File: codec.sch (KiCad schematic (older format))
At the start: 15 parts, among them U4 TLV320AIC3101

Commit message: Use a better codec
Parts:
- removed TP1: MIC1LP/LINE1LP, symbol Connector:TestPoint_Probe
- removed TP2: HPLCOM, symbol Connector:TestPoint_Probe
- removed TP3: HPLOUT, symbol Connector:TestPoint_Probe
- removed TP4: LEFT_LOM, symbol Connector:TestPoint_Probe
- removed TP5: LEFT_LOP, symbol Connector:TestPoint_Probe
- removed U4: TLV320AIC3101, Package_DFN_QFN:QFN-32-1EP_5x5mm_P0.5mm_EP3.65x3.65mm, symbol Audio:TLV320AIC3101
- added C13: 0.1u, symbol Device:C
- added C14: 1u, symbol Device:C
- added C15: 10u, symbol Device:C
- added U2: WM8731SEDS, Package_SO:SSOP-28_5.3x10.2mm_P0.65mm, symbol Audio:WM8731SEDS
- C10, C12: value 1u -> 10u
- C11: value 0.1u -> 10u
- C6: value 1u -> 0.1u
- C8: value 10u -> 1u
- C9: value 0.1u -> 1u
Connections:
- net labels added: ADC, AVDD, DAC, DBVDD, DCVDD, HPVDD, SCLK, SDIN, ~CSB
- net labels removed: 1.8V, DIN, DOUT, SCL, SDA, ~RESET
- no-connect marks 10 -> 9

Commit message: Various fixes
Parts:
- added R18: 10k, symbol Device:R
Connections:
- net 3.3V: now also R18.2; no longer U2.21 (MODE)
- new net: R18.1, U2.21 (MODE)
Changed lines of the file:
@@
 Wire Wire Line
 	5250 3950 5400 3950
-Text GLabel 5250 4250 0    50   Input ~ 0
-3.3V
-Wire Wire Line
-	5250 4250 5400 4250
+Text GLabel 4400 4250 0    50   Input ~ 0
+3.3V
 Text GLabel 1950 2650 0    50   Input ~ 0
 3.3V
@@
 Wire Wire Line
 	6300 3050 6300 3150
+$Comp
+L Device:R R18
+U 1 1 6039A986
+P 4650 4250
+F 0 "R18" V 4443 4250 50  0000 C CNN
+F 1 "10k" V 4534 4250 50  0000 C CNN
+F 2 "" V 4580 4250 50  0001 C CNN
+F 3 "~" H 4650 4250 50  0001 C CNN
+	1    4650 4250
+	0    1    1    0
+$EndComp
+Wire Wire Line
+	4500 4250 4400 4250
+Wire Wire Line
+	4800 4250 5400 4250
 $EndSCHEMATC

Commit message: Add debug interface
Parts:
- renumbered C13 to C21, C4 to C22, C5 to C23, C6 to C24, C14 to C25, C7 to C26, C8 to C27, C9 to C28, C15 to C29, C10 to C30, C11 to C31, C12 to C32, R18 to R19, U2 to U4
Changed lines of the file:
@@
 $EndDescr
 $Comp
-L Audio:WM8731SEDS U2
+L Audio:WM8731SEDS U4
 U 1 1 6005E3AC
 P 6100 4050
-F 0 "U2" H 5250 5100 50  0000 C CNN
+F 0 "U4" H 5250 5100 50  0000 C CNN
 F 1 "WM8731SEDS" H 5450 5000 50  0000 C CNN
 F 2 "Package_SO:SSOP-28_5.3x10.2mm_P0.65mm" H 6100 2750 50  0001 C CNN
@@
 $EndComp
 $Comp
-L power:GND #PWR07
+L power:GND #PWR035
 U 1 1 60067126
 P 5900 5050
-F 0 "#PWR07" H 5900 4800 50  0001 C CNN
+F 0 "#PWR035" H 5900 4800 50  0001 C CNN
 F 1 "GND" H 5905 4877 50  0000 C CNN
 F 2 "" H 5900 5050 50  0001 C CNN
@@
 Connection ~ 6200 5000
 $Comp
-L Device:C C13
+L Device:C C21
 U 1 1 600750C8
 P 2100 2900
-F 0 "C13" H 2215 2946 50  0000 L CNN
+F 0 "C21" H 2215 2946 50  0000 L CNN
 F 1 "0.1u" H 2215 2855 50  0000 L CNN
 F 2 "" H 2138 2750 50  0001 C CNN
@@
 $EndComp
 $Comp
-L Device:C C14
+L Device:C C25
 U 1 1 600750CE
 P 2550 2900
-F 0 "C14" H 2665 2946 50  0000 L CNN
+F 0 "C25" H 2665 2946 50  0000 L CNN
 F 1 "1u" H 2665 2855 50  0000 L CNN
 F 2 "" H 2588 2750 50  0001 C CNN
@@
 	2100 2650 2550 2650
 $Comp
-L Device:C C15
+L Device:C C29
 U 1 1 600750DE
 P 3000 2900
-F 0 "C15" H 3115 2946 50  0000 L CNN
+F 0 "C29" H 3115 2946 50  0000 L CNN
 F 1 "10u" H 3115 2855 50  0000 L CNN
 F 2 "" H 3038 2750 50  0001 C CNN
@@
 Connection ~ 2100 2650
 $Comp
-L power:GND #PWR08
+L power:GND #PWR031
 U 1 1 600DD992
 P 2550 3200
-F 0 "#PWR08" H 2550 2950 50  0001 C CNN
+F 0 "#PWR031" H 2550 2950 50  0001 C CNN
 F 1 "GND" H 2555 3027 50  0000 C CNN
 F 2 "" H 2550 3200 50  0001 C CNN
@@
 	5900 3050 5900 3150
 $Comp
-L Device:C C4
+L Device:C C22
 U 1 1 600E70B7
 P 2100 3800
-F 0 "C4" H 2215 3846 50  0000 L CNN
+F 0 "C22" H 2215 3846 50  0000 L CNN
 F 1 "0.1u" H 2215 3755 50  0000 L CNN
 F 2 "" H 2138 3650 50  0001 C CNN
@@
 $EndComp
 $Comp
-L Device:C C7
+L Device:C C26
 U 1 1 600E70BD
 P 2550 3800
-F 0 "C7" H 2665 3846 50  0000 L CNN
+F 0 "C26" H 2665 3846 50  0000 L CNN
 F 1 "1u" H 2665 3755 50  0000 L CNN
 F 2 "" H 2588 3650 50  0001 C CNN
@@
 	2100 3550 2550 3550
 $Comp
-L Device:C C10
+L Device:C C30
 U 1 1 600E70C9
 P 3000 3800
-F 0 "C10" H 3115 3846 50  0000 L CNN
+F 0 "C30" H 3115 3846 50  0000 L CNN
 F 1 "10u" H 3115 3755 50  0000 L CNN
 F 2 "" H 3038 3650 50  0001 C CNN
@@
 Connection ~ 2100 3550
 $Comp
-L power:GND #PWR09
+L power:GND #PWR032
 U 1 1 600E70D8
 P 2550 4100
-F 0 "#PWR09" H 2550 3850 50  0001 C CNN
+F 0 "#PWR032" H 2550 3850 50  0001 C CNN
 F 1 "GND" H 2555 3927 50  0000 C CNN
 F 2 "" H 2550 4100 50  0001 C CNN
@@
 Connection ~ 3000 3550
 $Comp
-L Device:C C5
+L Device:C C23
 U 1 1 600EA2F4
 P 2100 4700
-F 0 "C5" H 2215 4746 50  0000 L CNN
+F 0 "C23" H 2215 4746 50  0000 L CNN
 F 1 "0.1u" H 2215 4655 50  0000 L CNN
 F 2 "" H 2138 4550 50  0001 C CNN
@@
 $EndComp
 $Comp
-L Device:C C8
+L Device:C C27
 U 1 1 600EA2FA
 P 2550 4700
-F 0 "C8" H 2665 4746 50  0000 L CNN
+F 0 "C27" H 2665 4746 50  0000 L CNN
 F 1 "1u" H 2665 4655 50  0000 L CNN
 F 2 "" H 2588 4550 50  0001 C CNN
@@
 	2100 4450 2550 4450
 $Comp
-L Device:C C11
+L Device:C C31
 U 1 1 600EA306
 P 3000 4700
-F 0 "C11" H 3115 4746 50  0000 L CNN
+F 0 "C31" H 3115 4746 50  0000 L CNN
 F 1 "10u" H 3115 4655 50  0000 L CNN
 F 2 "" H 3038 4550 50  0001 C CNN
@@
 Connection ~ 2100 4450
 $Comp
-L power:GND #PWR011
+L power:GND #PWR033
 U 1 1 600EA315
 P 2550 5000
-F 0 "#PWR011" H 2550 4750 50  0001 C CNN
+F 0 "#PWR033" H 2550 4750 50  0001 C CNN
 F 1 "GND" H 2555 4827 50  0000 C CNN
 F 2 "" H 2550 5000 50  0001 C CNN
@@
 Connection ~ 3000 4450
 $Comp
-L Device:C C6
+L Device:C C24
 U 1 1 600F07D0
 P 2100 5600
-F 0 "C6" H 2215 5646 50  0000 L CNN
+F 0 "C24" H 2215 5646 50  0000 L CNN
 F 1 "0.1u" H 2215 5555 50  0000 L CNN
 F 2 "" H 2138 5450 50  0001 C CNN
@@
 $EndComp
 $Comp
-L Device:C C9
+L Device:C C28
 U 1 1 600F07D6
 P 2550 5600
-F 0 "C9" H 2665 5646 50  0000 L CNN
+F 0 "C28" H 2665 5646 50  0000 L CNN
 F 1 "1u" H 2665 5555 50  0000 L CNN
 F 2 "" H 2588 5450 50  0001 C CNN
@@
 	2100 5350 2550 5350
 $Comp
-L Device:C C12
+L Device:C C32
 U 1 1 600F07E2
 P 3000 5600
-F 0 "C12" H 3115 5646 50  0000 L CNN
+F 0 "C32" H 3115 5646 50  0000 L CNN
 F 1 "10u" H 3115 5555 50  0000 L CNN
 F 2 "" H 3038 5450 50  0001 C CNN
@@
 Connection ~ 2100 5350
 $Comp
-L power:GND #PWR012
+L power:GND #PWR034
 U 1 1 600F07F1
 P 2550 5900
-F 0 "#PWR012" H 2550 5650 50  0001 C CNN
+F 0 "#PWR034" H 2550 5650 50  0001 C CNN
 F 1 "GND" H 2555 5727 50  0000 C CNN
 F 2 "" H 2550 5900 50  0001 C CNN
@@
 	6300 3050 6300 3150
 $Comp
-L Device:R R18
+L Device:R R19
 U 1 1 6039A986
 P 4650 4250
-F 0 "R18" V 4443 4250 50  0000 C CNN
+F 0 "R19" V 4443 4250 50  0000 C CNN
 F 1 "10k" V 4534 4250 50  0000 C CNN
 F 2 "" V 4580 4250 50  0001 C CNN

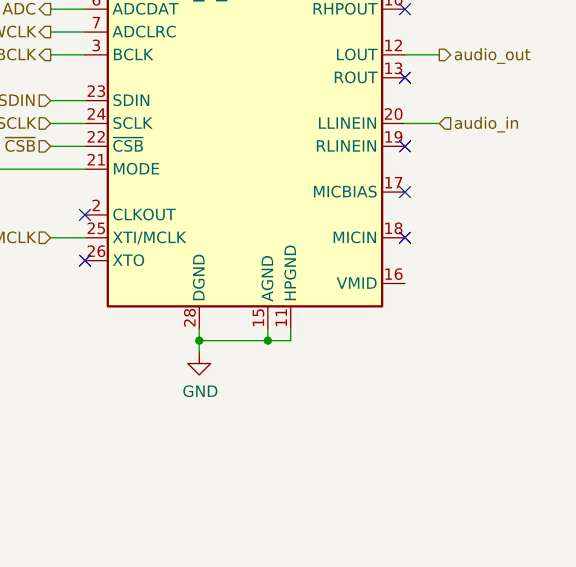
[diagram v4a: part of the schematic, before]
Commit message: Improved probe points
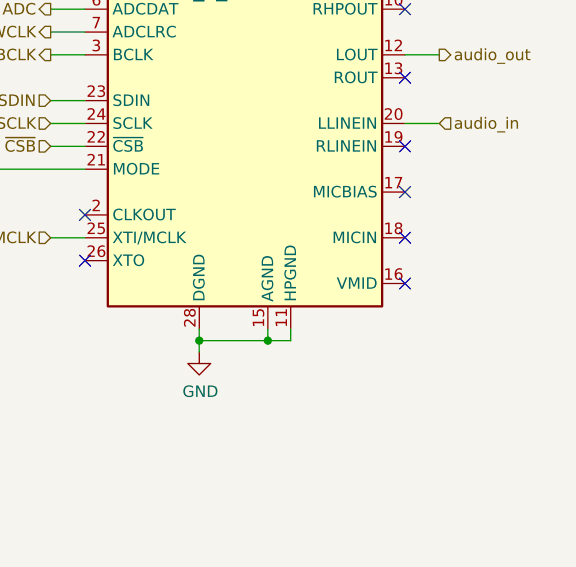
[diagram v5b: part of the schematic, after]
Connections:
- no-connect marks 9 -> 10
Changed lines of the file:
@@
 $EndComp
 $Comp
-L power:GND #PWR036
+L power:GND #PWR044
 U 1 1 60067126
 P 5900 5050
-F 0 "#PWR036" H 5900 4800 50  0001 C CNN
+F 0 "#PWR044" H 5900 4800 50  0001 C CNN
 F 1 "GND" H 5905 4877 50  0000 C CNN
 F 2 "" H 5900 5050 50  0001 C CNN
@@
 Connection ~ 2100 2650
 $Comp
-L power:GND #PWR032
+L power:GND #PWR040
 U 1 1 600DD992
 P 2550 3200
-F 0 "#PWR032" H 2550 2950 50  0001 C CNN
+F 0 "#PWR040" H 2550 2950 50  0001 C CNN
 F 1 "GND" H 2555 3027 50  0000 C CNN
 F 2 "" H 2550 3200 50  0001 C CNN
@@
 Connection ~ 2100 3550
 $Comp
-L power:GND #PWR033
+L power:GND #PWR041
 U 1 1 600E70D8
 P 2550 4100
-F 0 "#PWR033" H 2550 3850 50  0001 C CNN
+F 0 "#PWR041" H 2550 3850 50  0001 C CNN
 F 1 "GND" H 2555 3927 50  0000 C CNN
 F 2 "" H 2550 4100 50  0001 C CNN
@@
 Connection ~ 2100 4450
 $Comp
-L power:GND #PWR034
+L power:GND #PWR042
 U 1 1 600EA315
 P 2550 5000
-F 0 "#PWR034" H 2550 4750 50  0001 C CNN
+F 0 "#PWR042" H 2550 4750 50  0001 C CNN
 F 1 "GND" H 2555 4827 50  0000 C CNN
 F 2 "" H 2550 5000 50  0001 C CNN
@@
 Connection ~ 2100 5350
 $Comp
-L power:GND #PWR035
+L power:GND #PWR043
 U 1 1 600F07F1
 P 2550 5900
-F 0 "#PWR035" H 2550 5650 50  0001 C CNN
+F 0 "#PWR043" H 2550 5650 50  0001 C CNN
 F 1 "GND" H 2555 5727 50  0000 C CNN
 F 2 "" H 2550 5900 50  0001 C CNN
@@
 Wire Wire Line
 	4800 4250 5400 4250
+NoConn ~ 6800 4750
 $EndSCHEMATC

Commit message: Assign a bunch of footprints
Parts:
- C21, C22, C23, C24, C25, C26, C27, C28, C29, C30, C31, C32: footprint (none) -> Capacitor_SMD:C_0603_1608Metric
- R19: footprint (none) -> Resistor_SMD:R_0603_1608Metric
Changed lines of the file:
@@
 F 0 "C21" H 2215 2946 50  0000 L CNN
 F 1 "0.1u" H 2215 2855 50  0000 L CNN
-F 2 "" H 2138 2750 50  0001 C CNN
+F 2 "Capacitor_SMD:C_0603_1608Metric" H 2138 2750 50  0001 C CNN
 F 3 "~" H 2100 2900 50  0001 C CNN
 	1    2100 2900
@@
 F 0 "C25" H 2665 2946 50  0000 L CNN
 F 1 "1u" H 2665 2855 50  0000 L CNN
-F 2 "" H 2588 2750 50  0001 C CNN
+F 2 "Capacitor_SMD:C_0603_1608Metric" H 2588 2750 50  0001 C CNN
 F 3 "~" H 2550 2900 50  0001 C CNN
 	1    2550 2900
@@
 F 0 "C29" H 3115 2946 50  0000 L CNN
 F 1 "10u" H 3115 2855 50  0000 L CNN
-F 2 "" H 3038 2750 50  0001 C CNN
+F 2 "Capacitor_SMD:C_0603_1608Metric" H 3038 2750 50  0001 C CNN
 F 3 "~" H 3000 2900 50  0001 C CNN
 	1    3000 2900
@@
 F 0 "C22" H 2215 3846 50  0000 L CNN
 F 1 "0.1u" H 2215 3755 50  0000 L CNN
-F 2 "" H 2138 3650 50  0001 C CNN
+F 2 "Capacitor_SMD:C_0603_1608Metric" H 2138 3650 50  0001 C CNN
 F 3 "~" H 2100 3800 50  0001 C CNN
 	1    2100 3800
@@
 F 0 "C26" H 2665 3846 50  0000 L CNN
 F 1 "1u" H 2665 3755 50  0000 L CNN
-F 2 "" H 2588 3650 50  0001 C CNN
+F 2 "Capacitor_SMD:C_0603_1608Metric" H 2588 3650 50  0001 C CNN
 F 3 "~" H 2550 3800 50  0001 C CNN
 	1    2550 3800
@@
 F 0 "C30" H 3115 3846 50  0000 L CNN
 F 1 "10u" H 3115 3755 50  0000 L CNN
-F 2 "" H 3038 3650 50  0001 C CNN
+F 2 "Capacitor_SMD:C_0603_1608Metric" H 3038 3650 50  0001 C CNN
 F 3 "~" H 3000 3800 50  0001 C CNN
 	1    3000 3800
@@
 F 0 "C23" H 2215 4746 50  0000 L CNN
 F 1 "0.1u" H 2215 4655 50  0000 L CNN
-F 2 "" H 2138 4550 50  0001 C CNN
+F 2 "Capacitor_SMD:C_0603_1608Metric" H 2138 4550 50  0001 C CNN
 F 3 "~" H 2100 4700 50  0001 C CNN
 	1    2100 4700
@@
 F 0 "C27" H 2665 4746 50  0000 L CNN
 F 1 "1u" H 2665 4655 50  0000 L CNN
-F 2 "" H 2588 4550 50  0001 C CNN
+F 2 "Capacitor_SMD:C_0603_1608Metric" H 2588 4550 50  0001 C CNN
 F 3 "~" H 2550 4700 50  0001 C CNN
 	1    2550 4700
@@
 F 0 "C31" H 3115 4746 50  0000 L CNN
 F 1 "10u" H 3115 4655 50  0000 L CNN
-F 2 "" H 3038 4550 50  0001 C CNN
+F 2 "Capacitor_SMD:C_0603_1608Metric" H 3038 4550 50  0001 C CNN
 F 3 "~" H 3000 4700 50  0001 C CNN
 	1    3000 4700
@@
 F 0 "C24" H 2215 5646 50  0000 L CNN
 F 1 "0.1u" H 2215 5555 50  0000 L CNN
-F 2 "" H 2138 5450 50  0001 C CNN
+F 2 "Capacitor_SMD:C_0603_1608Metric" H 2138 5450 50  0001 C CNN
 F 3 "~" H 2100 5600 50  0001 C CNN
 	1    2100 5600
@@
 F 0 "C28" H 2665 5646 50  0000 L CNN
 F 1 "1u" H 2665 5555 50  0000 L CNN
-F 2 "" H 2588 5450 50  0001 C CNN
+F 2 "Capacitor_SMD:C_0603_1608Metric" H 2588 5450 50  0001 C CNN
 F 3 "~" H 2550 5600 50  0001 C CNN
 	1    2550 5600
@@
 F 0 "C32" H 3115 5646 50  0000 L CNN
 F 1 "10u" H 3115 5555 50  0000 L CNN
-F 2 "" H 3038 5450 50  0001 C CNN
+F 2 "Capacitor_SMD:C_0603_1608Metric" H 3038 5450 50  0001 C CNN
 F 3 "~" H 3000 5600 50  0001 C CNN
 	1    3000 5600
@@
 F 0 "R19" V 4443 4250 50  0000 C CNN
 F 1 "10k" V 4534 4250 50  0000 C CNN
-F 2 "" V 4580 4250 50  0001 C CNN
+F 2 "Resistor_SMD:R_0603_1608Metric" V 4580 4250 50  0001 C CNN
 F 3 "~" H 4650 4250 50  0001 C CNN
 	1    4650 4250

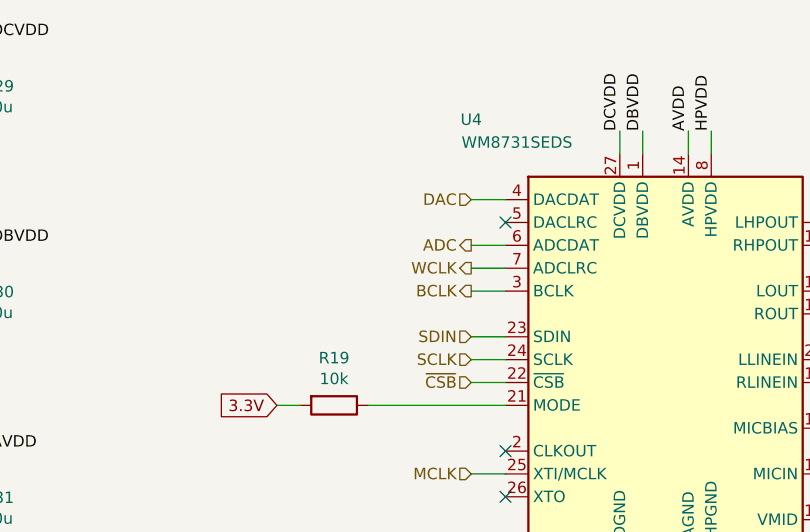
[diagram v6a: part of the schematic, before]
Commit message: those two need to be connected
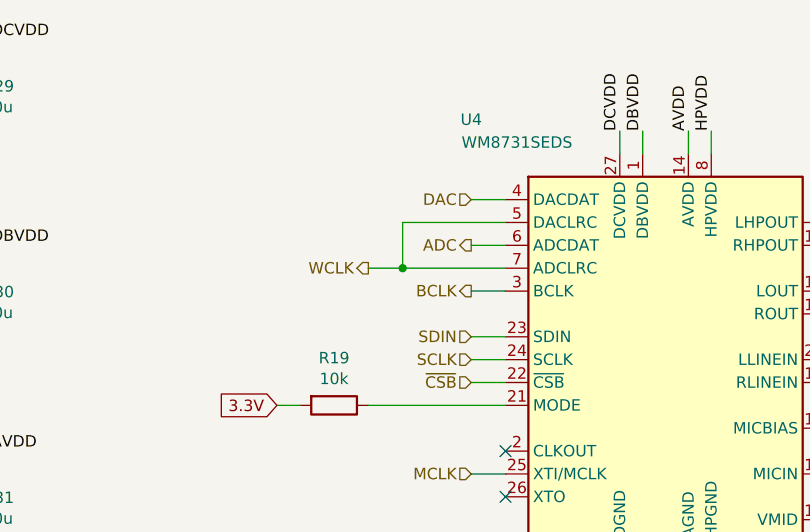
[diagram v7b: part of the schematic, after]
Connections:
- net WCLK: now also U4.5 (DACLRC)
- no-connect marks 10 -> 9
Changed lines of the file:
@@
 Wire Wire Line
 	5250 3750 5400 3750
-Text HLabel 5250 3650 0    50   Output ~ 0
+Text HLabel 4800 3650 0    50   Output ~ 0
 WCLK
 Wire Wire Line
-	5250 3650 5400 3650
+	4800 3650 4950 3650
 Text HLabel 5250 3350 0    50   Input ~ 0
 DAC
@@
 Wire Wire Line
 	5250 3550 5400 3550
-NoConn ~ 5400 3450
 Text HLabel 5250 4050 0    50   Input ~ 0
 SCLK
@@
 	4800 4250 5400 4250
 NoConn ~ 6800 4750
+Wire Wire Line
+	4950 3650 4950 3450
+Wire Wire Line
+	4950 3450 5400 3450
+Connection ~ 4950 3650
+Wire Wire Line
+	4950 3650 5400 3650
 $EndSCHEMATC

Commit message: just a buncha stuff
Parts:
- removed C25, C26, C27, C28: 1u, Capacitor_SMD:C_0603_1608Metric, symbol Device:C
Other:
- moved on the sheet: C29, C30, C31, C32
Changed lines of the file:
@@
 	1    0    0    -1
 $EndComp
-$Comp
-L Device:C C25
-U 1 1 600750CE
+Wire Wire Line
+	2100 2650 2100 2750
+Wire Wire Line
+	2100 3050 2100 3100
+Wire Wire Line
+	2100 3100 2550 3100
+$Comp
+L Device:C C29
+U 1 1 600750DE
 P 2550 2900
-F 0 "C25" H 2665 2946 50  0000 L CNN
-F 1 "1u" H 2665 2855 50  0000 L CNN
+F 0 "C29" H 2665 2946 50  0000 L CNN
+F 1 "10u" H 2665 2855 50  0000 L CNN
 F 2 "Capacitor_SMD:C_0603_1608Metric" H 2588 2750 50  0001 C CNN
 F 3 "~" H 2550 2900 50  0001 C CNN
@@
 $EndComp
 Wire Wire Line
-	2550 2650 2550 2750
-Wire Wire Line
-	2100 2650 2100 2750
-Wire Wire Line
-	2100 3050 2100 3100
-Wire Wire Line
 	2550 3100 2550 3050
 Wire Wire Line
-	2100 3100 2550 3100
-Wire Wire Line
-	2100 2650 2550 2650
-$Comp
-L Device:C C29
-U 1 1 600750DE
-P 3000 2900
-F 0 "C29" H 3115 2946 50  0000 L CNN
-F 1 "10u" H 3115 2855 50  0000 L CNN
-F 2 "Capacitor_SMD:C_0603_1608Metric" H 3038 2750 50  0001 C CNN
-F 3 "~" H 3000 2900 50  0001 C CNN
-	1    3000 2900
-	1    0    0    -1
-$EndComp
-Wire Wire Line
-	2550 3100 3000 3100
-Wire Wire Line
-	3000 3100 3000 3050
-Connection ~ 2550 3100
-Wire Wire Line
-	3000 2750 3000 2650
-Wire Wire Line
-	3000 2650 2550 2650
-Connection ~ 2550 2650
+	2550 2750 2550 2650
 NoConn ~ 5400 4450
 NoConn ~ 6800 3450
@@
 Wire Wire Line
 	1950 2650 2100 2650
-Connection ~ 2100 2650
 $Comp
 L power:GND #PWR040
@@
 Wire Wire Line
 	2550 3200 2550 3100
-Text Label 3150 2650 0    50   ~ 0
+Text Label 2700 2650 0    50   ~ 0
 DCVDD
 Wire Wire Line
-	3150 2650 3000 2650
-Connection ~ 3000 2650
+	2700 2650 2550 2650
 Text Label 5900 3050 1    50   ~ 0
 DCVDD
@@
 	1    0    0    -1
 $EndComp
-$Comp
-L Device:C C26
-U 1 1 600E70BD
+Wire Wire Line
+	2100 3550 2100 3650
+Wire Wire Line
+	2100 3950 2100 4000
+Wire Wire Line
+	2100 4000 2550 4000
+$Comp
+L Device:C C30
+U 1 1 600E70C9
 P 2550 3800
-F 0 "C26" H 2665 3846 50  0000 L CNN
-F 1 "1u" H 2665 3755 50  0000 L CNN
+F 0 "C30" H 2665 3846 50  0000 L CNN
+F 1 "10u" H 2665 3755 50  0000 L CNN
 F 2 "Capacitor_SMD:C_0603_1608Metric" H 2588 3650 50  0001 C CNN
 F 3 "~" H 2550 3800 50  0001 C CNN
@@
 $EndComp
 Wire Wire Line
-	2550 3550 2550 3650
-Wire Wire Line
-	2100 3550 2100 3650
-Wire Wire Line
-	2100 3950 2100 4000
-Wire Wire Line
 	2550 4000 2550 3950
 Wire Wire Line
-	2100 4000 2550 4000
-Wire Wire Line
-	2100 3550 2550 3550
-$Comp
-L Device:C C30
-U 1 1 600E70C9
-P 3000 3800
-F 0 "C30" H 3115 3846 50  0000 L CNN
-F 1 "10u" H 3115 3755 50  0000 L CNN
-F 2 "Capacitor_SMD:C_0603_1608Metric" H 3038 3650 50  0001 C CNN
-F 3 "~" H 3000 3800 50  0001 C CNN
-	1    3000 3800
-	1    0    0    -1
-$EndComp
-Wire Wire Line
-	2550 4000 3000 4000
-Wire Wire Line
-	3000 4000 3000 3950
-Connection ~ 2550 4000
-Wire Wire Line
-	3000 3650 3000 3550
-Wire Wire Line
-	3000 3550 2550 3550
-Connection ~ 2550 3550
+	2550 3650 2550 3550
 Text GLabel 1950 3550 0    50   Input ~ 0
 3.3V
 Wire Wire Line
 	1950 3550 2100 3550
-Connection ~ 2100 3550
 $Comp
 L power:GND #PWR041
@@
 Wire Wire Line
 	2550 4100 2550 4000
-Text Label 3150 3550 0    50   ~ 0
+Text Label 2700 3550 0    50   ~ 0
 DBVDD
 Wire Wire Line
-	3150 3550 3000 3550
-Connection ~ 3000 3550
+	2700 3550 2550 3550
 $Comp
 L Device:C C23
@@
 	1    0    0    -1
 $EndComp
-$Comp
-L Device:C C27
-U 1 1 600EA2FA
+Wire Wire Line
+	2100 4450 2100 4550
+Wire Wire Line
+	2100 4850 2100 4900
+Wire Wire Line
+	2100 4900 2550 4900
+$Comp
+L Device:C C31
+U 1 1 600EA306
 P 2550 4700
-F 0 "C27" H 2665 4746 50  0000 L CNN
-F 1 "1u" H 2665 4655 50  0000 L CNN
+F 0 "C31" H 2665 4746 50  0000 L CNN
+F 1 "10u" H 2665 4655 50  0000 L CNN
 F 2 "Capacitor_SMD:C_0603_1608Metric" H 2588 4550 50  0001 C CNN
 F 3 "~" H 2550 4700 50  0001 C CNN
@@
 $EndComp
 Wire Wire Line
-	2550 4450 2550 4550
-Wire Wire Line
-	2100 4450 2100 4550
-Wire Wire Line
-	2100 4850 2100 4900
-Wire Wire Line
 	2550 4900 2550 4850
 Wire Wire Line
-	2100 4900 2550 4900
-Wire Wire Line
-	2100 4450 2550 4450
-$Comp
-L Device:C C31
-U 1 1 600EA306
-P 3000 4700
-F 0 "C31" H 3115 4746 50  0000 L CNN
-F 1 "10u" H 3115 4655 50  0000 L CNN
-F 2 "Capacitor_SMD:C_0603_1608Metric" H 3038 4550 50  0001 C CNN
-F 3 "~" H 3000 4700 50  0001 C CNN
-	1    3000 4700
-	1    0    0    -1
-$EndComp
-Wire Wire Line
-	2550 4900 3000 4900
-Wire Wire Line
-	3000 4900 3000 4850
-Connection ~ 2550 4900
-Wire Wire Line
-	3000 4550 3000 4450
-Wire Wire Line
-	3000 4450 2550 4450
-Connection ~ 2550 4450
+	2550 4550 2550 4450
 Text GLabel 1950 4450 0    50   Input ~ 0
 3.3V
 Wire Wire Line
 	1950 4450 2100 4450
-Connection ~ 2100 4450
 $Comp
 L power:GND #PWR042
@@
 Wire Wire Line
 	2550 5000 2550 4900
-Text Label 3150 4450 0    50   ~ 0
+Text Label 2700 4450 0    50   ~ 0
 AVDD
 Wire Wire Line
-	3150 4450 3000 4450
-Connection ~ 3000 4450
+	2700 4450 2550 4450
 $Comp
 L Device:C C24
@@
 	1    0    0    -1
 $EndComp
-$Comp
-L Device:C C28
-U 1 1 600F07D6
+Wire Wire Line
+	2100 5350 2100 5450
+Wire Wire Line
+	2100 5750 2100 5800
+Wire Wire Line
+	2100 5800 2550 5800
+$Comp
+L Device:C C32
+U 1 1 600F07E2
 P 2550 5600
-F 0 "C28" H 2665 5646 50  0000 L CNN
-F 1 "1u" H 2665 5555 50  0000 L CNN
+F 0 "C32" H 2665 5646 50  0000 L CNN
+F 1 "10u" H 2665 5555 50  0000 L CNN
 F 2 "Capacitor_SMD:C_0603_1608Metric" H 2588 5450 50  0001 C CNN
 F 3 "~" H 2550 5600 50  0001 C CNN
@@
 $EndComp
 Wire Wire Line
-	2550 5350 2550 5450
-Wire Wire Line
-	2100 5350 2100 5450
-Wire Wire Line
-	2100 5750 2100 5800
-Wire Wire Line
 	2550 5800 2550 5750
 Wire Wire Line
-	2100 5800 2550 5800
-Wire Wire Line
-	2100 5350 2550 5350
-$Comp
-L Device:C C32
-U 1 1 600F07E2
-P 3000 5600
-F 0 "C32" H 3115 5646 50  0000 L CNN
-F 1 "10u" H 3115 5555 50  0000 L CNN
-F 2 "Capacitor_SMD:C_0603_1608Metric" H 3038 5450 50  0001 C CNN
-F 3 "~" H 3000 5600 50  0001 C CNN
-	1    3000 5600
-	1    0    0    -1
-$EndComp
-Wire Wire Line
-	2550 5800 3000 5800
-Wire Wire Line
-	3000 5800 3000 5750
-Connection ~ 2550 5800
-Wire Wire Line
-	3000 5450 3000 5350
-Wire Wire Line
-	3000 5350 2550 5350
-Connection ~ 2550 5350
+	2550 5450 2550 5350
 Text GLabel 1950 5350 0    50   Input ~ 0
 3.3V
 Wire Wire Line
 	1950 5350 2100 5350
-Connection ~ 2100 5350
 $Comp
 L power:GND #PWR043
@@
 Wire Wire Line
 	2550 5900 2550 5800
-Text Label 3150 5350 0    50   ~ 0
+Text Label 2700 5350 0    50   ~ 0
 HPVDD
 Wire Wire Line
-	3150 5350 3000 5350
-Connection ~ 3000 5350
+	2700 5350 2550 5350
 Text Label 6000 3050 1    50   ~ 0
 DBVDD
@@
 Wire Wire Line
 	4950 3650 5400 3650
+Connection ~ 2550 3100
+Wire Wire Line
+	2100 2650 2550 2650
+Connection ~ 2100 2650
+Connection ~ 2550 2650
+Connection ~ 2550 4000
+Wire Wire Line
+	2550 3550 2100 3550
+Connection ~ 2550 3550
+Connection ~ 2100 3550
+Connection ~ 2550 4900
+Wire Wire Line
+	2550 4450 2100 4450
+Connection ~ 2550 4450
+Connection ~ 2100 4450
+Connection ~ 2550 5800
+Wire Wire Line
+	2550 5350 2100 5350
+Connection ~ 2550 5350
+Connection ~ 2100 5350
 $EndSCHEMATC
